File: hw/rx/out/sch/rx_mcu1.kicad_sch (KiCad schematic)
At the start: 21 parts, among them J2 SWD, U1 BT40E

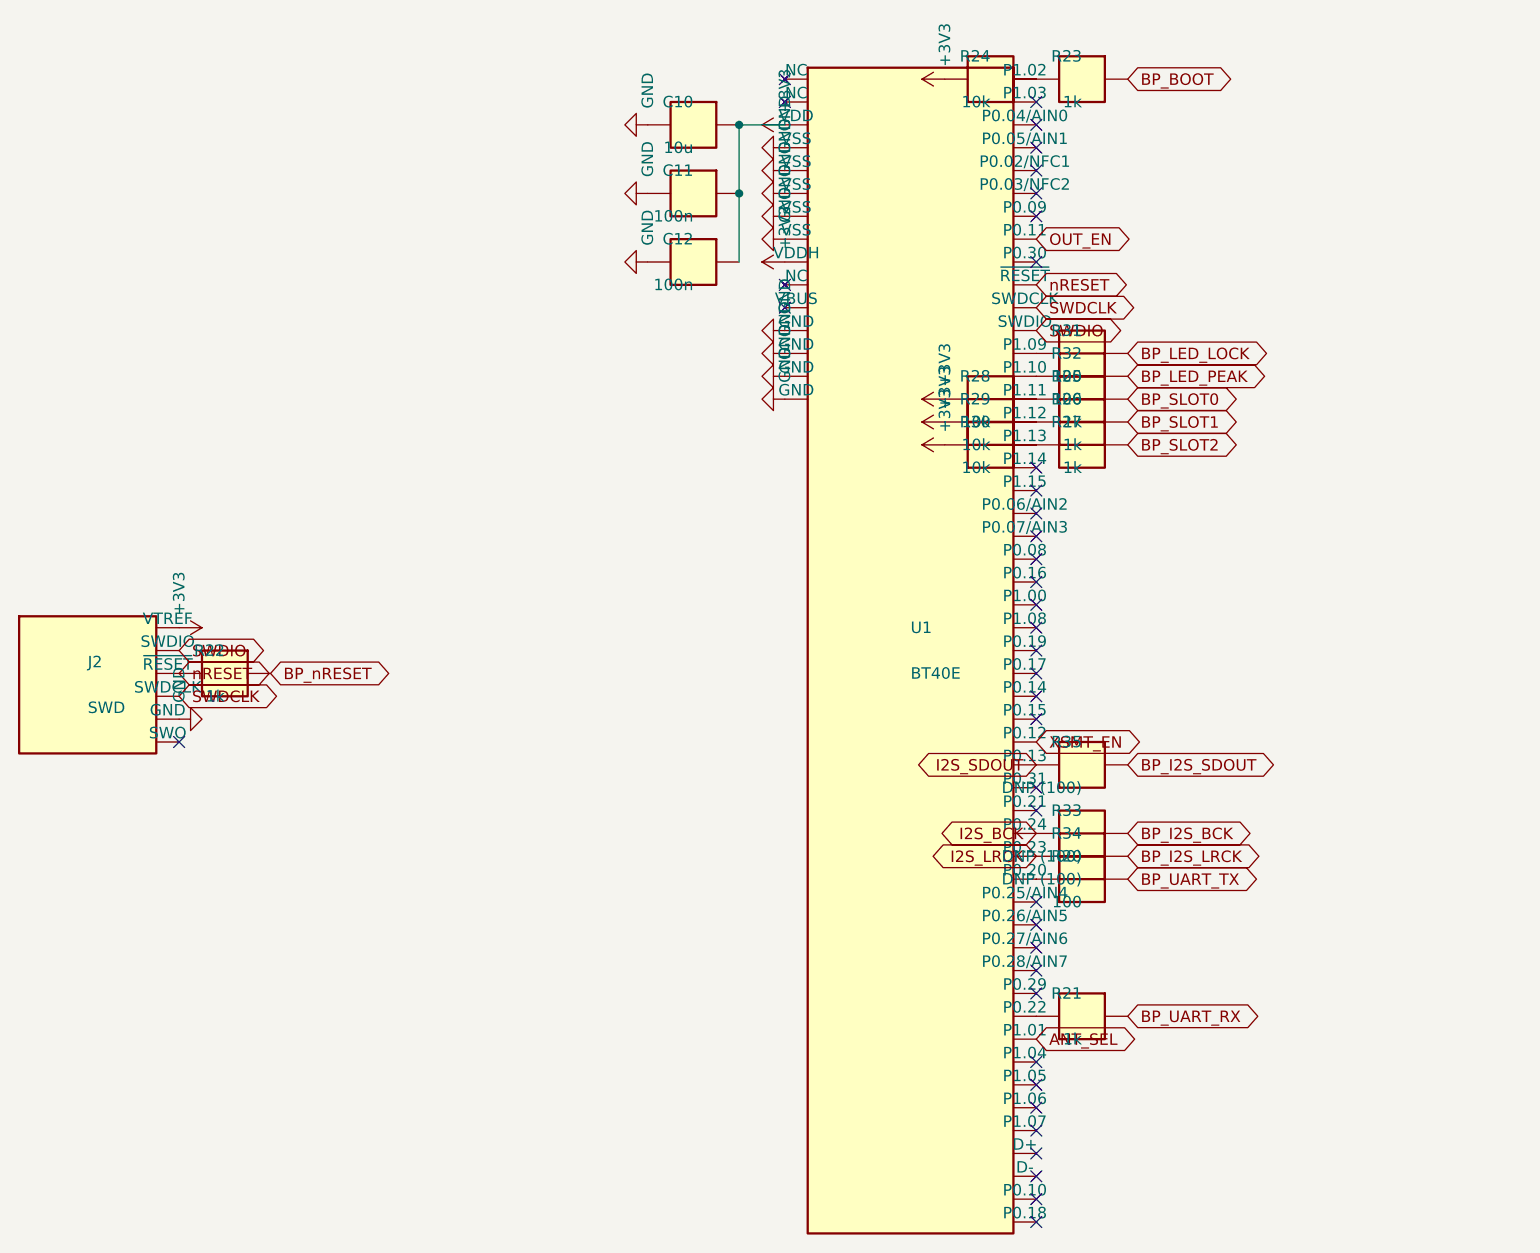
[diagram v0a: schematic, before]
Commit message: hw/rx: BT40E + TQ2SA footprints, THT underside backplane header, bring-up test points (#34)
Co-Authored-By: Claude Opus 5.5 <noreply@anthropic.com>
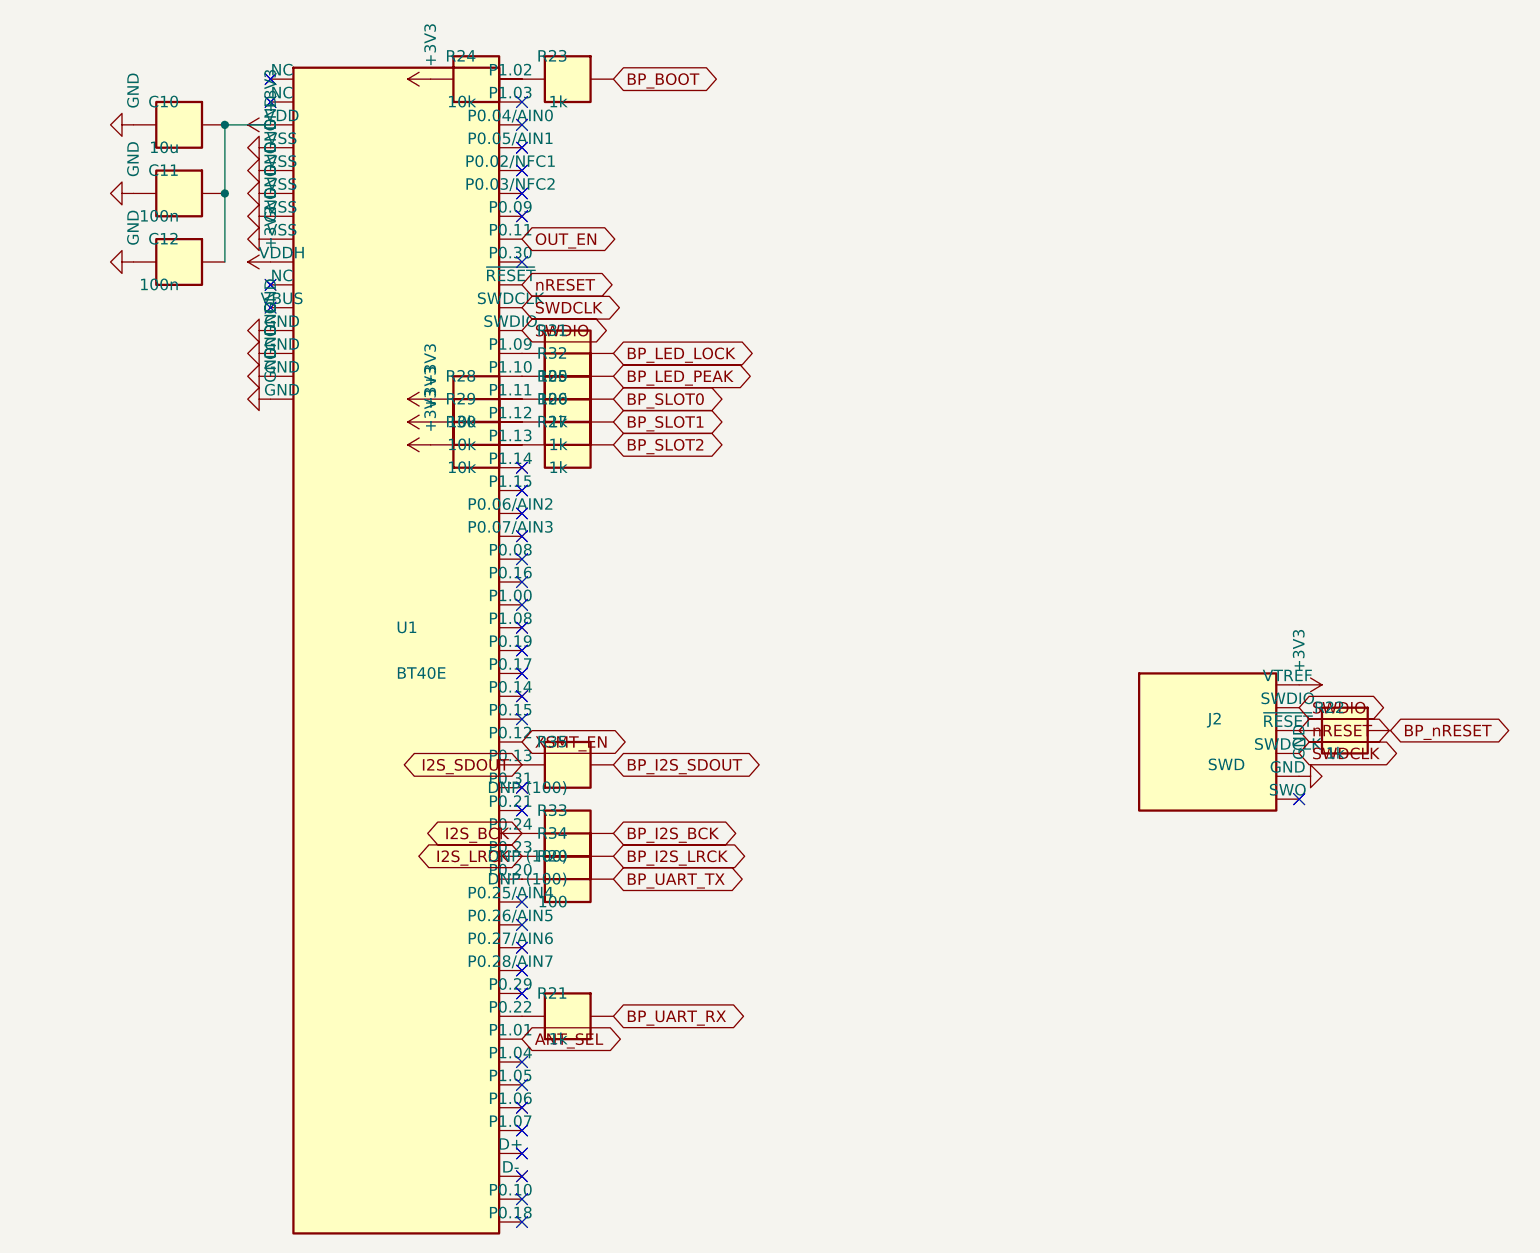
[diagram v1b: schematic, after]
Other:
- moved on the sheet: C10, C11, C12, J2, R20, R21, R22, R23, R24, R25, R26, R27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
